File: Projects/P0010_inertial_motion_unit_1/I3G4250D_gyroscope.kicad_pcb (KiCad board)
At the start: 2 copper layers, 33 x 33 mm, 23 parts, among them J1 modular8_rev3_comms_in, J2 modular8_rev3_comms_out, U1 I3G4250DTR, U2 ADXL343

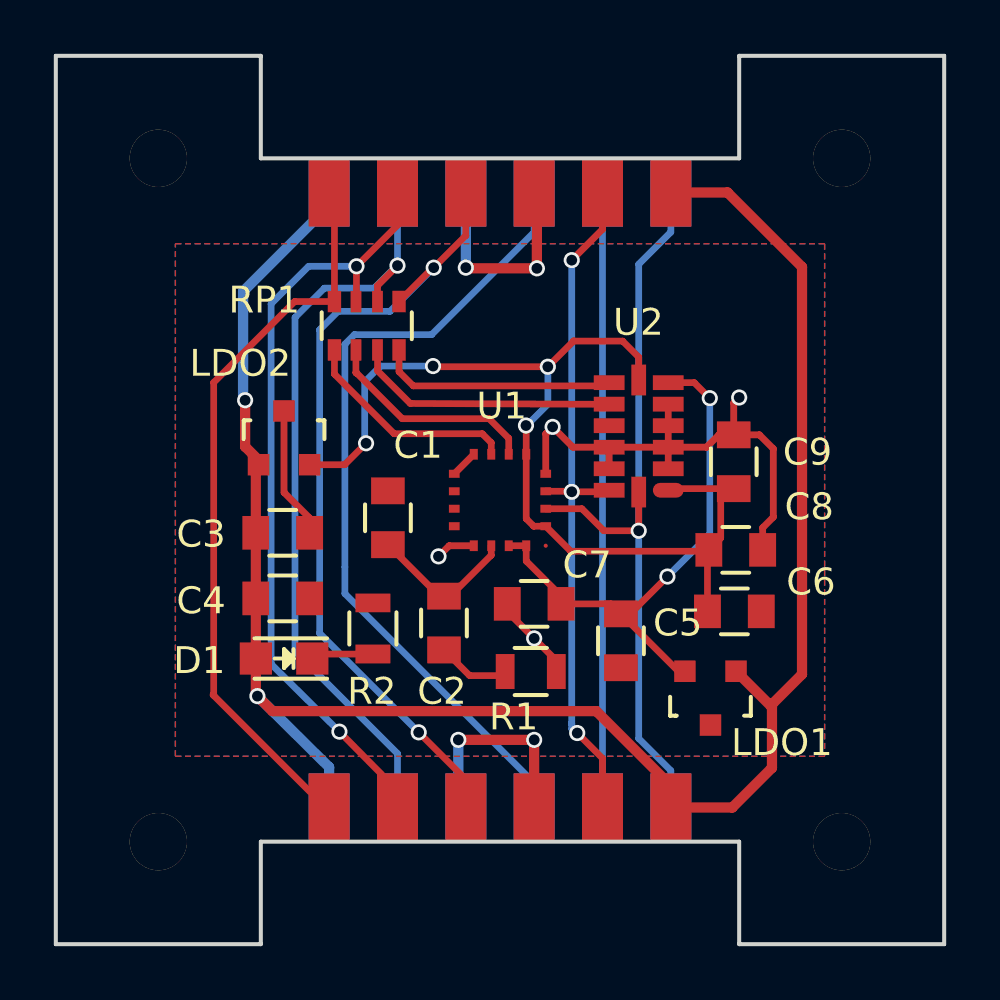
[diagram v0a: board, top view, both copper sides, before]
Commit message: moved gyro/accel to Projects
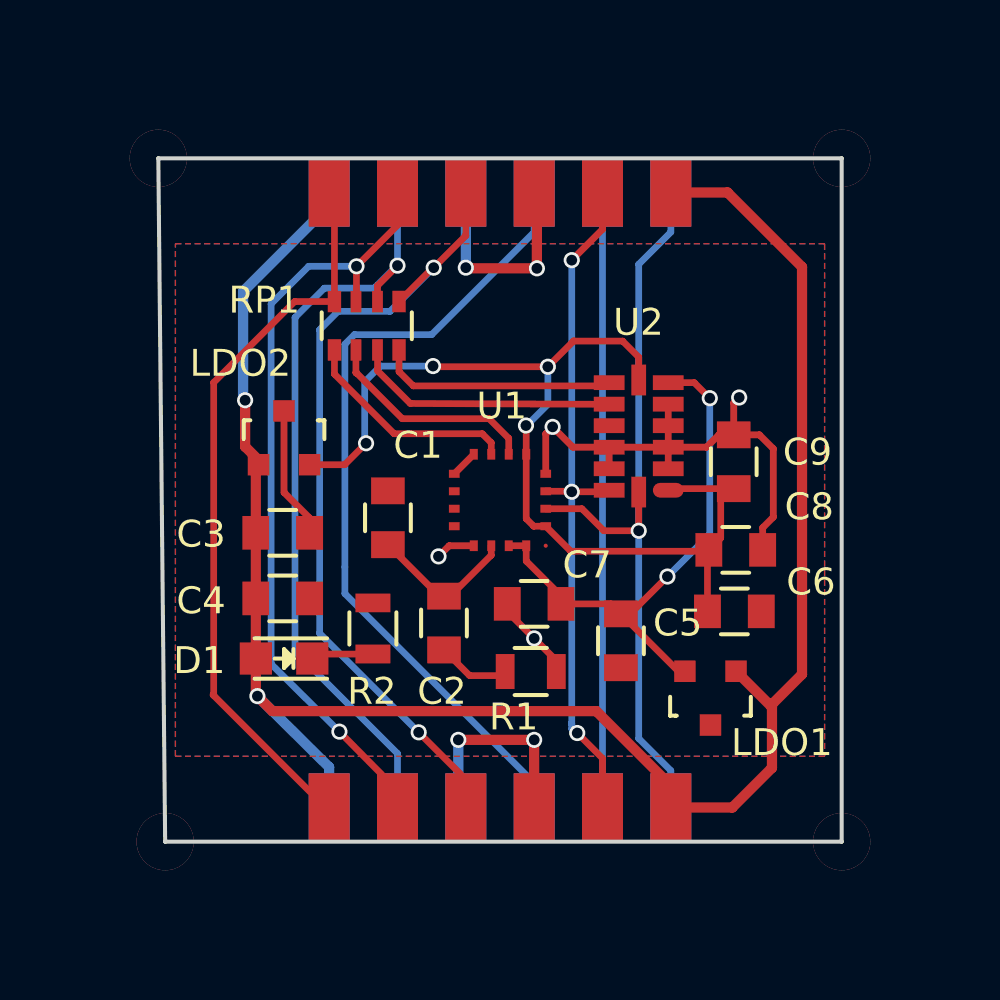
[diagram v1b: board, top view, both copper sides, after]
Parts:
- removed the REF** at (152.4, 101.6)
- removed the REF** at (127.0, 101.6)
- removed the REF** at (127.0, 76.2)
- removed the REF** at (152.4, 76.2)
- added REF**: modular8_mounting_hole, open_robotics:modular8_mounting_hole, F.Cu at (127.0, 76.2)
- added REF**: modular8_mounting_hole, open_robotics:modular8_mounting_hole, F.Cu at (152.4, 76.2)
- added REF**: modular8_mounting_hole, open_robotics:modular8_mounting_hole, F.Cu at (152.4, 101.6)
- added REF**: modular8_mounting_hole, open_robotics:modular8_mounting_hole, F.Cu at (127.3, 101.6)
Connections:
- LDO1 pad 1: +5V -> Net-(LDO1-Pad1)
- LDO1 pad 2: +3.3VP -> Net-(LDO1-Pad2)
- LDO1 pad 3: GND -> Net-(LDO1-Pad3)
- LDO2 pad 1: +5V -> Net-(LDO2-Pad1)
- LDO2 pad 2: +3V3 -> Net-(LDO2-Pad2)
- LDO2 pad 3: GND -> Net-(LDO2-Pad3)
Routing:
- net Net-(LDO2-Pad2): track 0.00 -> 4.74 mm, vias 0 -> 1
- net +3V3: track 37.4 -> 32.7 mm, vias 4 -> 3
- net Net-(LDO2-Pad3): track 0.00 -> 3.03 mm
- net GND: track 46.3 -> 43.3 mm
- net +5V: track 75.9 -> 73.0 mm
- net Net-(LDO1-Pad1): track 0.00 -> 1.89 mm
- net Net-(LDO2-Pad1): track 0.00 -> 1.02 mm
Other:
- board size 33 x 33 mm -> 25.4 x 25.4 mm
- board text added: "IG34250D gyroscope ADXL343 accelerometer I2C breakout 3.3V logic 2.048/3.3v scale analog out"
- board text added: "Max Prokopenko"
- board text added: "modular8.com/0010"
- board text added: "openrobotics.ca"
- board text added: "rev1"

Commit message: generated gerbers, ordered P0010
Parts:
- C1, C2, C3, C4, C5, C6, C7, C8, C9: footprint Capacitors_SMD:C_0805 -> Capacitors_SMD:C_0603
- J1, J2: footprint Libraries - KiCAD:modular8_rev3_edge -> open_robotics:modular8_rev3_edge
- R1, R2: footprint Resistors_SMD:R_0805 -> Resistors_SMD:R_0603
- U1: footprint Libraries - KiCAD:LGA-16 -> open_robotics:LGA-16
- U2: footprint Libraries - KiCAD:LGACC-14-1 -> open_robotics:LGACC-14-1
- moved REF** 0.25 mm to (127.0, 101.6)
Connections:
- LDO1 pad 1: Net-(LDO1-Pad1) -> +5V
- LDO1 pad 2: Net-(LDO1-Pad2) -> +3.3VP
- LDO1 pad 3: Net-(LDO1-Pad3) -> GND
- LDO2 pad 1: Net-(LDO2-Pad1) -> +5V
- LDO2 pad 2: Net-(LDO2-Pad2) -> +3V3
- LDO2 pad 3: Net-(LDO2-Pad3) -> GND
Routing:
- net Net-(LDO2-Pad2): track 4.74 -> 0.00 mm, vias 1 -> 0
- net +3V3: track 32.7 -> 37.4 mm, vias 3 -> 4
- net Net-(LDO2-Pad3): track 3.03 -> 0.00 mm
- net GND: track 43.3 -> 46.3 mm
- net +5V: track 73.0 -> 75.9 mm
- net Net-(LDO1-Pad1): track 1.89 -> 0.00 mm
- net Net-(LDO2-Pad1): track 1.02 -> 0.00 mm
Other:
- outline, holes or cut-outs redrawn
- board text added: "IG34250D gyroscope ADXL343 accelerometer I2C breakout 5V power 3.3V logic"
- board text removed: "IG34250D gyroscope ADXL343 accelerometer I2C breakout 3.3V logic 2.048/3.3v scale analog out"
